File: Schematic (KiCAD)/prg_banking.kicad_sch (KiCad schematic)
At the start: 76 parts

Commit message: Schematic and SVG Updates
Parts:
- removed A50: NOR_2, symbol MMC5:NOR_2
- added A50: NAND_2, symbol MMC5:NAND_2
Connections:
- net +M2_CLK_BUF3{A38}: now also A50. (X)
- net /PRG_ROM_CE_PIN: now also A50. (X)
- net at E29. (X): now also E30. (X); no longer E28. (X)
- net at E22. (X): now also E21. (X); no longer E26. (/Q)
- net at A48. (X): now also A54. (X); no longer A49. (X)
- net at B90. (X): now also A51. (X); no longer B92. (X)
- net at A52. (X): now also A50. (X)
- net at D21. (X): now also A27. (Y1); no longer D20. (X)
- net at D25. (X): now also D26. (X); no longer D24. (X)
- net at D26. (X): now also A24. (Y1); no longer D25. (X)
- new net: B38. (Y2), D34. (X)
- new net: A25. (Y1), D22. (X)
- new net: A34. (Y4), A35. (Y4), A36. (Y4), D37. (X)
- new net: E26. (/Q), E28. (X)
- new net: E28. (X), E29. (X)
- new net: A22. (Y4), A23. (Y2), A37. (Y4), D30. (X)
- new net: E22. (X), E26. (/Q)
- new net: D32. (X), D33. (X)
- new net: D16. (X), D32. (X)
- new net: A48. (X), A49. (X)
- new net: A48. (X), A51. (X)
- new net: B90. (X), B92. (X)
- new net: D4. (Q1), D9. (X)
- new net: A52. (X), A53. (X)
- new net: A29. (Y4), A30. (Y4), A31. (Y4), D31. (X)
- new net: D17. (X), D18. (X)
- new net: D20. (X), D21. (X)
- new net: D19. (X), D20. (X)
- new net: A41. (X), A42. (X), A43. (X)
- new net: D27. (X), D29. (X)
- new net: D11. (X), D4. (Q1)
- new net: D28. (X), D29. (X)
- new net: A45. (X), A49. (X), A53. (X)
- new net: A32. (Y5), A33. (Y5), D36. (X)
- new net: D24. (X), D25. (X)
- new net: D23. (X), D25. (X)
- new net: D15. (X), D23. (X)
- new net: A43. (X), A44. (X), A47. (X)
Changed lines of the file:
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@@
 	)
 	(symbol
-		(lib_id "MMC5:NOR_2")
-		(at 325.12 21.59 0)
-		(unit 1)
-		(exclude_from_sim no)
-		(in_bom yes)
-		(on_board yes)
-		(dnp no)
-		(fields_autoplaced yes)
-		(property "Reference" "A50"
-			(at 325.12 17.272 0)
-			(do_not_autoplace yes)
-			(effects
-				(font
-					(size 1.27 1.27)
-				)
-				(justify top)
-			)
-		)
-		(property "Value" "NOR_2"
-			(at 325.12 21.59 0)
-			(do_not_autoplace yes)
-			(effects
-				(font
-					(size 0.635 0.635)
-				)
-			)
-		)
-		(property "Footprint" ""
-			(at 325.12 21.59 0)
-			(effects
-				(font
-					(size 1.27 1.27)
-				)
-				(hide yes)
-			)
-		)
-		(property "Datasheet" ""
-			(at 325.12 21.59 0)
-			(effects
-				(font
-					(size 1.27 1.27)
-				)
-				(hide yes)
-			)
-		)
-		(property "Description" ""
-			(at 325.12 21.59 0)
-			(effects
-				(font
-					(size 1.27 1.27)
-				)
-				(hide yes)
-			)
-		)
-		(pin ""
-		)
-		(pin ""
-		)
-		(pin ""
-		)
-		(instances
-			(project ""
-				(path "/46093bf6-f83e-4237-9ece-7350a682aff0/592254d1-b82c-4794-a868-544fd8c831b6"
-					(reference "A50")
-					(unit 1)
-				)
-			)
-		)
-	)
-	(symbol
 		(lib_name "INVERT_16")
 		(lib_id "MMC5:INVERT")
@@
 					(unit 1)
 				)
+			)
+		)
+	)
+	(symbol
+		(lib_name "NAND_2_19")
+		(lib_id "MMC5:NAND_2")
+		(at 325.12 21.59 0)
+		(unit 1)
+		(exclude_from_sim no)
+		(in_bom yes)
+		(on_board yes)
+		(dnp no)
+		(fields_autoplaced yes)
+		(property "Reference" "A50"
+			(at 325.12 17.272 0)
+			(do_not_autoplace yes)
+			(effects
+				(font
+					(size 1.27 1.27)
+				)
+				(justify top)
+			)
+		)
+		(property "Value" "NAND_2"
+			(at 325.12 21.59 0)
+			(do_not_autoplace yes)
+			(effects
+				(font
+					(size 0.635 0.635)
+				)
+			)
+		)
+		(property "Footprint" ""
+			(at 325.12 21.59 0)
+			(effects
+				(font
+					(size 1.27 1.27)
+				)
+				(hide yes)
+			)
+		)
+		(property "Datasheet" ""
+			(at 325.12 21.59 0)
+			(effects
+				(font
+					(size 1.27 1.27)
+				)
+				(hide yes)
+			)
+		)
+		(property "Description" ""
+			(at 325.12 21.59 0)
+			(effects
+				(font
+					(size 1.27 1.27)
+				)
+				(hide yes)
+			)
+		)
+		(pin ""
+		)
+		(pin ""
+		)
+		(pin ""
+		)
+		(instances
+			(project "MMC5"
+				(path "/46093bf6-f83e-4237-9ece-7350a682aff0/592254d1-b82c-4794-a868-544fd8c831b6"
+					(reference "A50")
+					(unit 1)
+				)

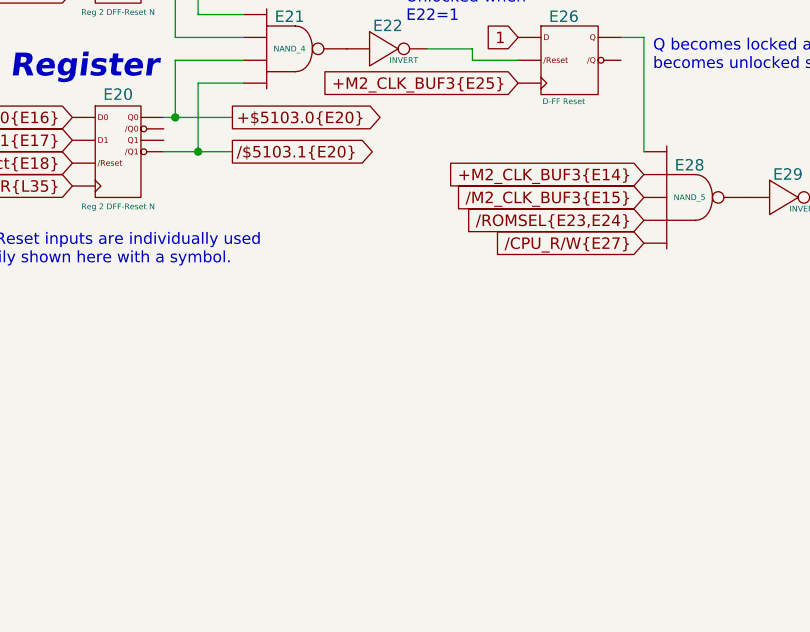
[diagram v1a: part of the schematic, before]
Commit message: Tracing and schematic updates.  - Added timer to schematic.  - Added all items from artifacts sheet to the MMC5A trace.
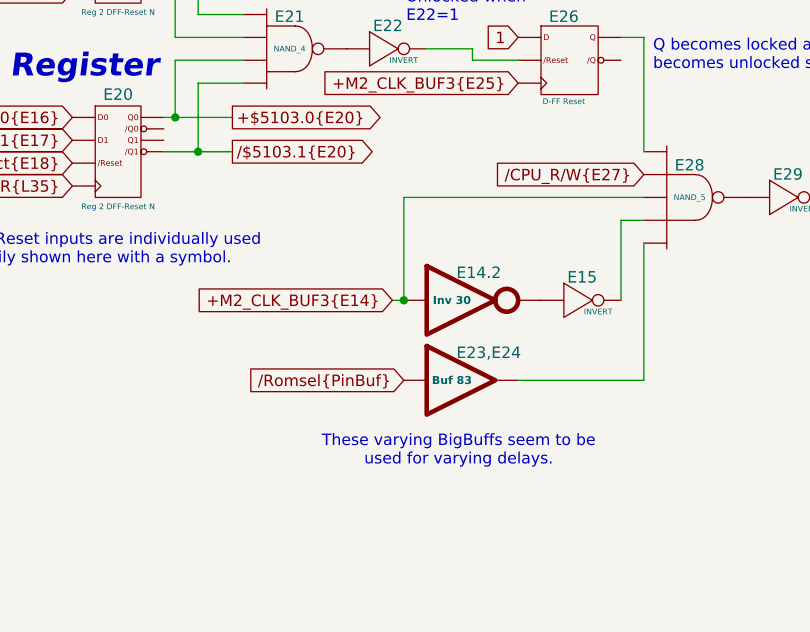
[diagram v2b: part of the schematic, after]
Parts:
- added E14.2: Inv 30, symbol MMC5:BIGINV
- added E15: INVERT, symbol MMC5:INVERT
- added E23,E24: Buf 83, symbol MMC5:BIGBUF
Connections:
- net /M2_CLK_BUF3{E15} is gone; now on net /CPU_R/W{E27}: E28. (X)
- net /ROMSEL{E23,E24} is gone; now on net /CPU_R/W{E27}: E28. (X)
- net +M2_CLK_BUF3{E14}: now also E14.2. (X)
- net at E29. (X): now also E30. (X); no longer E28. (X)
- net at E22. (X): now also E21. (X); no longer E26. (/Q)
- net at A48. (X): now also A54. (X); no longer A49. (X)
- net at B90. (X): now also A51. (X); no longer B92. (X)
- net at A52. (X): now also A50. (X); no longer A53. (X)
- net at D21. (X): now also A27. (Y1); no longer D20. (X)
- net at D25. (X): now also D26. (X); no longer D24. (X)
- net at D26. (X): now also A24. (Y1); no longer D25. (X)
- new net: B38. (Y2), D34. (X)
- new net: A25. (Y1), D22. (X)
- new net: A34. (Y4), A35. (Y4), A36. (Y4), D37. (X)
- new net: E26. (/Q), E28. (X)
- new net: E23,E24. (X), E28. (X)
- new net: E28. (X), E29. (X)
- new net: E15. (X), E28. (X)
- new net: A22. (Y4), A23. (Y2), A37. (Y4), D30. (X)
- new net: E22. (X), E26. (/Q)
- new net: D32. (X), D33. (X)
- new net: D16. (X), D32. (X)
- new net: A48. (X), A49. (X)
- new net: A48. (X), A51. (X)
- new net: B90. (X), B92. (X)
- new net: D4. (Q1), D9. (X)
- new net: A52. (X), A53. (X)
- new net: A29. (Y4), A30. (Y4), A31. (Y4), D31. (X)
- new net: D17. (X), D18. (X)
- new net: D20. (X), D21. (X)
- new net: D19. (X), D20. (X)
- new net: E14.2. (X), E15. (X)
- new net: A41. (X), A42. (X), A43. (X)
- new net: D27. (X), D29. (X)
- new net: D11. (X), D4. (Q1)
- new net: D28. (X), D29. (X)
- new net: A45. (X), A49. (X), A53. (X)
- new net: A32. (Y5), A33. (Y5), D36. (X)
- new net: D24. (X), D25. (X)
- new net: D23. (X), D25. (X)
- new net: D15. (X), D23. (X)
- new net: A43. (X), A44. (X), A47. (X)
- new net /Romsel{PinBuf}: E23,E24. (X)
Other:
- note added: "These varying BigBuffs seem to be used for varying delays."

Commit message: - Updated all of the various And-OR-Invert gates to have consistent names.  - Added the schematic for CL3 / SL3 GPIO pins.  There are no surprises revealed by this.  - Finished up the CPU address decoding tracing.  - Added one of the 'artifact' counters from the pulse channels
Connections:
- net at E29. (X): now also E30. (X); no longer E28. (X)
- net at E15. (X): now also E14.2. (X); no longer E28. (X)
- net at E22. (X): now also E21. (X); no longer E26. (/Q)
- net at A48. (X): now also A54. (X); no longer A49. (X)
- net at B90. (X): now also A51. (X); no longer B92. (X)
- net at A52. (X): now also A50. (X); no longer A53. (X)
- net at D21. (X): now also A27. (Y1); no longer D20. (X)
- net at D25. (X): now also D26. (X); no longer D24. (X)
- net at D26. (X): now also A24. (Y1); no longer D25. (X)
- new net: B38. (Y2), D34. (X)
- new net: A25. (Y1), D22. (X)
- new net: A34. (Y4), A35. (Y4), A36. (Y4), D37. (X)
- new net: E26. (/Q), E28. (X)
- new net: E23,E24. (X), E28. (X)
- new net: E28. (X), E29. (X)
- new net: E15. (X), E28. (X)
- new net: A22. (Y4), A23. (Y2), A37. (Y4), D30. (X)
- new net: E22. (X), E26. (/Q)
- new net: D32. (X), D33. (X)
- new net: D16. (X), D32. (X)
- new net: A48. (X), A49. (X)
- new net: A48. (X), A51. (X)
- new net: B90. (X), B92. (X)
- new net: D4. (Q1), D9. (X)
- new net: A52. (X), A53. (X)
- new net: A29. (Y4), A30. (Y4), A31. (Y4), D31. (X)
- new net: D17. (X), D18. (X)
- new net: D20. (X), D21. (X)
- new net: D19. (X), D20. (X)
- new net: A41. (X), A42. (X), A43. (X)
- new net: D27. (X), D29. (X)
- new net: D11. (X), D4. (Q1)
- new net: D28. (X), D29. (X)
- new net: A45. (X), A49. (X), A53. (X)
- new net: A32. (Y5), A33. (Y5), D36. (X)
- new net: D24. (X), D25. (X)
- new net: D23. (X), D25. (X)
- new net: D15. (X), D23. (X)
- new net: A43. (X), A44. (X), A47. (X)
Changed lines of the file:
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@@
 	)
 	(symbol
-		(lib_name "NAND_3_4")
 		(lib_id "MMC5:NAND_3")
 		(at 153.67 209.55 0)
@@
 	)
 	(symbol
-		(lib_name "TriBuf_1_1")
 		(lib_id "MMC5:TriBuf_1")
 		(at 190.5 83.82 0)
@@
 	)
 	(symbol
-		(lib_name "TriBuf_4_6")
 		(lib_id "MMC5:TriBuf_4")
 		(at 190.5 240.03 0)
@@
 	)
 	(symbol
-		(lib_name "Reg_8_D-Latch_2")
+		(lib_name "Reg_8_D-Latch_1")
 		(lib_id "MMC5:Reg_8_D-Latch")
 		(at 45.72 166.37 0)
@@
 	)
 	(symbol
-		(lib_name "INVERT_2")
 		(lib_id "MMC5:INVERT")
 		(at 68.58 43.18 0)
@@
 	)
 	(symbol
-		(lib_name "INVERT_4")
+		(lib_name "INVERT_7")
 		(lib_id "MMC5:INVERT")
 		(at 161.29 35.56 0)
@@
 	)
 	(symbol
-		(lib_name "D-FF_Reset_3")
 		(lib_id "MMC5:D-FF_Reset")
 		(at 332.74 130.81 0)
@@
 	)
 	(symbol
-		(lib_name "TriBuf_1_4")
+		(lib_name "TriBuf_1_2")
 		(lib_id "MMC5:TriBuf_1")
 		(at 190.5 118.11 0)
@@
 	)
 	(symbol
-		(lib_name "INVERT_17")
+		(lib_name "INVERT_19")
 		(lib_id "MMC5:INVERT")
 		(at 313.69 130.81 0)
@@
 	)
 	(symbol
-		(lib_name "NAND_2_9")
+		(lib_name "NAND_2_14")
 		(lib_id "MMC5:NAND_2")
 		(at 149.86 114.3 0)
@@
 	)
 	(symbol
-		(lib_name "NAND_2_15")
+		(lib_name "NAND_2_8")
 		(lib_id "MMC5:NAND_2")
 		(at 313.69 40.64 0)
@@
 	)
 	(symbol
-		(lib_name "NAND_3_7")
+		(lib_name "NAND_3_6")
 		(lib_id "MMC5:NAND_3")
 		(at 289.56 55.88 0)
@@
 	)
 	(symbol
-		(lib_name "INVERT_1")
+		(lib_name "INVERT_10")
 		(lib_id "MMC5:INVERT")
 		(at 59.69 27.94 0)
@@
 	)
 	(symbol
+		(lib_name "TriBuf_4_6")
 		(lib_id "MMC5:TriBuf_4")
 		(at 190.5 20.32 0)
@@
 	)
 	(symbol
-		(lib_name "INVERT_12")
+		(lib_name "INVERT_8")
 		(lib_id "MMC5:INVERT")
 		(at 313.69 26.67 0)
@@
 	)
 	(symbol
-		(lib_name "TriBuf_4_3")
+		(lib_name "TriBuf_4_5")
 		(lib_id "MMC5:TriBuf_4")
 		(at 190.5 128.27 0)
@@
 	)
 	(symbol
-		(lib_name "TriBuf_4_2")
+		(lib_name "TriBuf_4_1")
 		(lib_id "MMC5:TriBuf_4")
 		(at 190.5 158.75 0)
@@
 	)
 	(symbol
-		(lib_name "TriBuf_4_7")
+		(lib_name "TriBuf_4_4")
 		(lib_id "MMC5:TriBuf_4")
 		(at 190.5 224.79 0)
@@
 	)
 	(symbol
-		(lib_name "TriBuf_4_4")
+		(lib_name "TriBuf_4_3")
 		(lib_id "MMC5:TriBuf_4")
 		(at 190.5 143.51 0)
@@
 	)
 	(symbol
-		(lib_name "INVERT_9")
+		(lib_name "INVERT_11")
 		(lib_id "MMC5:INVERT")
 		(at 144.78 207.01 0)
@@
 	)
 	(symbol
-		(lib_name "NAND_2_6")
+		(lib_name "NAND_2_9")
 		(lib_id "MMC5:NAND_2")
 		(at 149.86 101.6 0)
@@
 	)
 	(symbol
-		(lib_name "INVERT_16")
+		(lib_name "INVERT_4")
 		(lib_id "MMC5:INVERT")
 		(at 289.56 86.36 0)
@@
 	)
 	(symbol
-		(lib_name "NAND_2_1")
+		(lib_name "NAND_2_6")
 		(lib_id "MMC5:NAND_2")
 		(at 133.35 27.94 0)
@@
 	)
 	(symbol
-		(lib_name "NAND_2_8")
+		(lib_name "NAND_2_1")
 		(lib_id "MMC5:NAND_2")
 		(at 161.29 115.57 0)
@@
 		(pin ""
 		)
+		(pin ""
+		)
+		(pin ""
+		)
 		(instances
 			(project ""
@@
 	)
 	(symbol
+		(lib_name "NAND_2_4")
 		(lib_id "MMC5:NAND_2")
 		(at 133.35 35.56 0)
@@
 	)
 	(symbol
-		(lib_name "INVERT_10")
+		(lib_name "INVERT_1")
 		(lib_id "MMC5:INVERT")
 		(at 289.56 25.4 0)
@@
 	)
 	(symbol
-		(lib_name "NAND_3_5")
+		(lib_name "NAND_3_2")
 		(lib_id "MMC5:NAND_3")
 		(at 133.35 243.84 0)
@@
 	)
 	(symbol
-		(lib_name "INVERT_8")
+		(lib_name "INVERT_9")
 		(lib_id "MMC5:INVERT")
 		(at 144.78 184.15 0)
@@
 	)
 	(symbol
-		(lib_name "NAND_2_14")
+		(lib_name "NAND_2_3")
 		(lib_id "MMC5:NAND_2")
 		(at 302.26 35.56 0)
@@
 	)
 	(symbol
-		(lib_name "NAND_2_3")
+		(lib_name "NAND_2_10")
 		(lib_id "MMC5:NAND_2")
 		(at 149.86 62.23 0)
@@
 	)
 	(symbol
-		(lib_name "NAND_3_1")
+		(lib_name "NAND_3_4")
 		(lib_id "MMC5:NAND_3")
 		(at 133.35 68.58 0)
@@
 	)
 	(symbol
-		(lib_name "NAND_2_10")
 		(lib_id "MMC5:NAND_2")
 		(at 133.35 113.03 0)
@@
 	)
 	(symbol
+		(lib_name "TriBuf_1_1")
 		(lib_id "MMC5:TriBuf_1")
 		(at 190.5 64.77 0)
@@
 	)
 	(symbol
-		(lib_name "TriBuf_4_5")
+		(lib_name "TriBuf_4_2")
 		(lib_id "MMC5:TriBuf_4")
 		(at 190.5 255.27 0)
@@
 	)
 	(symbol
-		(lib_name "NAND_2_16")
+		(lib_name "NAND_2_13")
 		(lib_id "MMC5:NAND_2")
 		(at 325.12 48.26 0)
@@
 	)
 	(symbol
-		(lib_name "NAND_2_4")
+		(lib_name "NAND_2_2")
 		(lib_id "MMC5:NAND_2")
 		(at 133.35 57.15 0)
@@
 	)
 	(symbol
-		(lib_name "NAND_2_18")
+		(lib_name "NAND_2_11")
 		(lib_id "MMC5:NAND_2")
 		(at 325.12 68.58 0)
@@
 	)
 	(symbol
-		(lib_name "INVERT_7")
+		(lib_name "INVERT_2")
 		(lib_id "MMC5:INVERT")
 		(at 161.29 101.6 0)
@@
 	)
 	(symbol
-		(lib_name "INVERT_14")
+		(lib_name "INVERT_3")
 		(lib_id "MMC5:INVERT")
 		(at 313.69 67.31 0)
@@
 	)
 	(symbol
-		(lib_name "NAND_2_2")
+		(lib_name "NAND_2_12")
 		(lib_id "MMC5:NAND_2")
 		(at 133.35 43.18 0)
@@
 	)
 	(symbol
-		(lib_name "INVERT_13")
+		(lib_name "INVERT_12")
 		(lib_id "MMC5:INVERT")
 		(at 300.99 55.88 0)
@@
 	)
 	(symbol
-		(lib_name "NAND_3_2")
+		(lib_name "NAND_3_3")
 		(lib_id "MMC5:NAND_3")
 		(at 133.35 81.28 0)
@@
 	)
 	(symbol
-		(lib_name "INVERT_19")
+		(lib_name "INVERT_17")
 		(lib_id "MMC5:INVERT")
 		(at 367.03 147.32 0)
@@
 	)
 	(symbol
-		(lib_name "NAND_3_3")
+		(lib_name "NAND_3_5")
 		(lib_id "MMC5:NAND_3")
 		(at 133.35 147.32 0)
@@
 	)
 	(symbol
-		(lib_name "TriBuf_1_2")
+		(lib_name "TriBuf_1_4")
 		(lib_id "MMC5:TriBuf_1")
 		(at 190.5 93.98 0)
@@
 	)
 	(symbol
-		(lib_name "NAND_2_13")
+		(lib_name "NAND_2_15")
 		(lib_id "MMC5:NAND_2")
 		(at 302.26 26.67 0)
@@
 	)
 	(symbol
-		(lib_name "NAND_3_6")
+		(lib_name "NAND_3_1")
 		(lib_id "MMC5:NAND_3")
 		(at 289.56 45.72 0)
@@
 	)
 	(symbol
-		(lib_name "TriBuf_4_1")
+		(lib_name "TriBuf_4_7")
 		(lib_id "MMC5:TriBuf_4")
 		(at 190.5 43.18 0)
@@
 	)
 	(symbol
+		(lib_name "NAND_3_7")
 		(lib_id "MMC5:NAND_3")
 		(at 149.86 35.56 0)
@@
 	)
 	(symbol
-		(lib_name "INVERT_11")
+		(lib_name "INVERT_13")
 		(lib_id "MMC5:INVERT")
 		(at 289.56 36.83 0)
@@
 	)
 	(symbol
-		(lib_name "NAND_2_12")
+		(lib_name "NAND_2_16")
 		(lib_id "MMC5:NAND_2")
 		(at 133.35 207.01 0)
@@
 	)
 	(symbol
-		(lib_name "INVERT_3")
+		(lib_name "INVERT_14")
 		(lib_id "MMC5:INVERT")
 		(at 68.58 33.02 0)
@@
 	)
 	(symbol
+		(lib_name "INVERT_15")
 		(lib_id "MMC5:INVERT")
 		(at 59.69 38.1 0)
@@
 	)
 	(symbol
-		(lib_name "Reg_8_D-Latch_1")
+		(lib_name "Reg_8_D-Latch_2")
 		(lib_id "MMC5:Reg_8_D-Latch")
 		(at 45.72 128.27 0)
@@
 	)
 	(symbol
-		(lib_name "TriBuf_5_1")
 		(lib_id "MMC5:TriBuf_5")
 		(at 190.5 190.5 0)
@@
 	)
 	(symbol
-		(lib_name "INVERT_109")
+		(lib_name "INVERT_20")
 		(lib_id "MMC5:INVERT")
 		(at 335.28 158.75 0)
@@
 	)
 	(symbol
+		(lib_name "TriBuf_5_1")
 		(lib_id "MMC5:TriBuf_5")
 		(at 190.5 173.99 0)
@@
 	)
 	(symbol
-		(lib_name "NAND_2_11")
+		(lib_name "NAND_2_18")
 		(lib_id "MMC5:NAND_2")
 		(at 133.35 184.15 0)
@@
 	)
 	(symbol
-		(lib_name "INVERT_15")
+		(lib_name "INVERT_16")
 		(lib_id "MMC5:INVERT")
 		(at 280.67 78.74 0)
